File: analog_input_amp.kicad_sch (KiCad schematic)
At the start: 39 parts, among them U301 THS4521ID

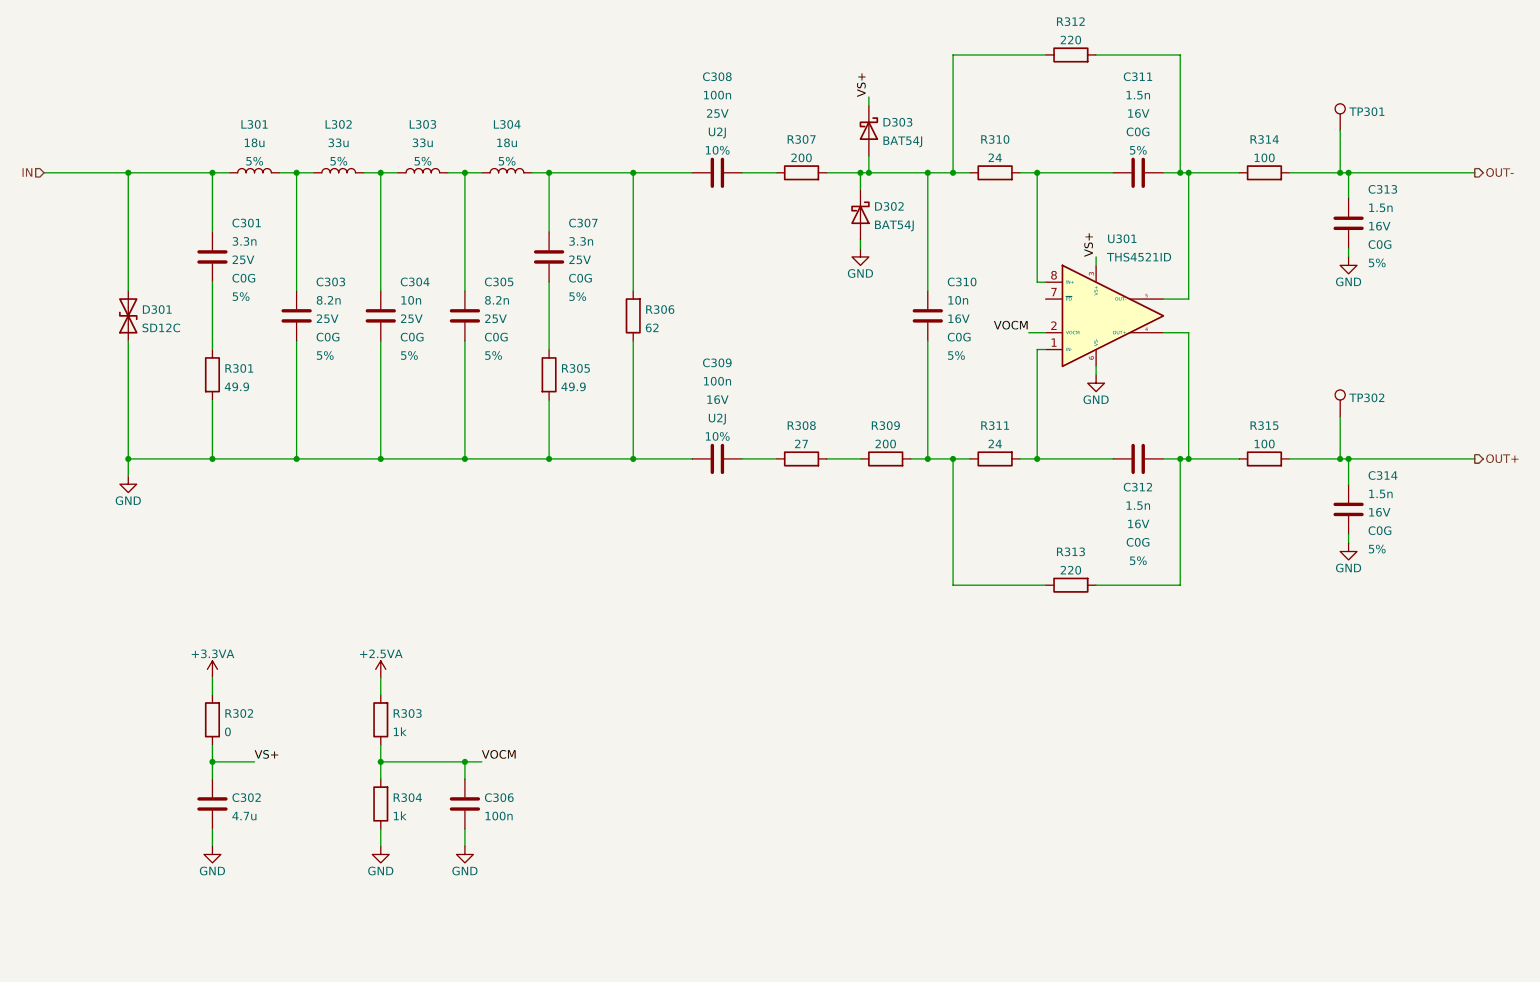
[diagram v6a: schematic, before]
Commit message: Schematic: better LDO output capacitor selection, clarified BOM
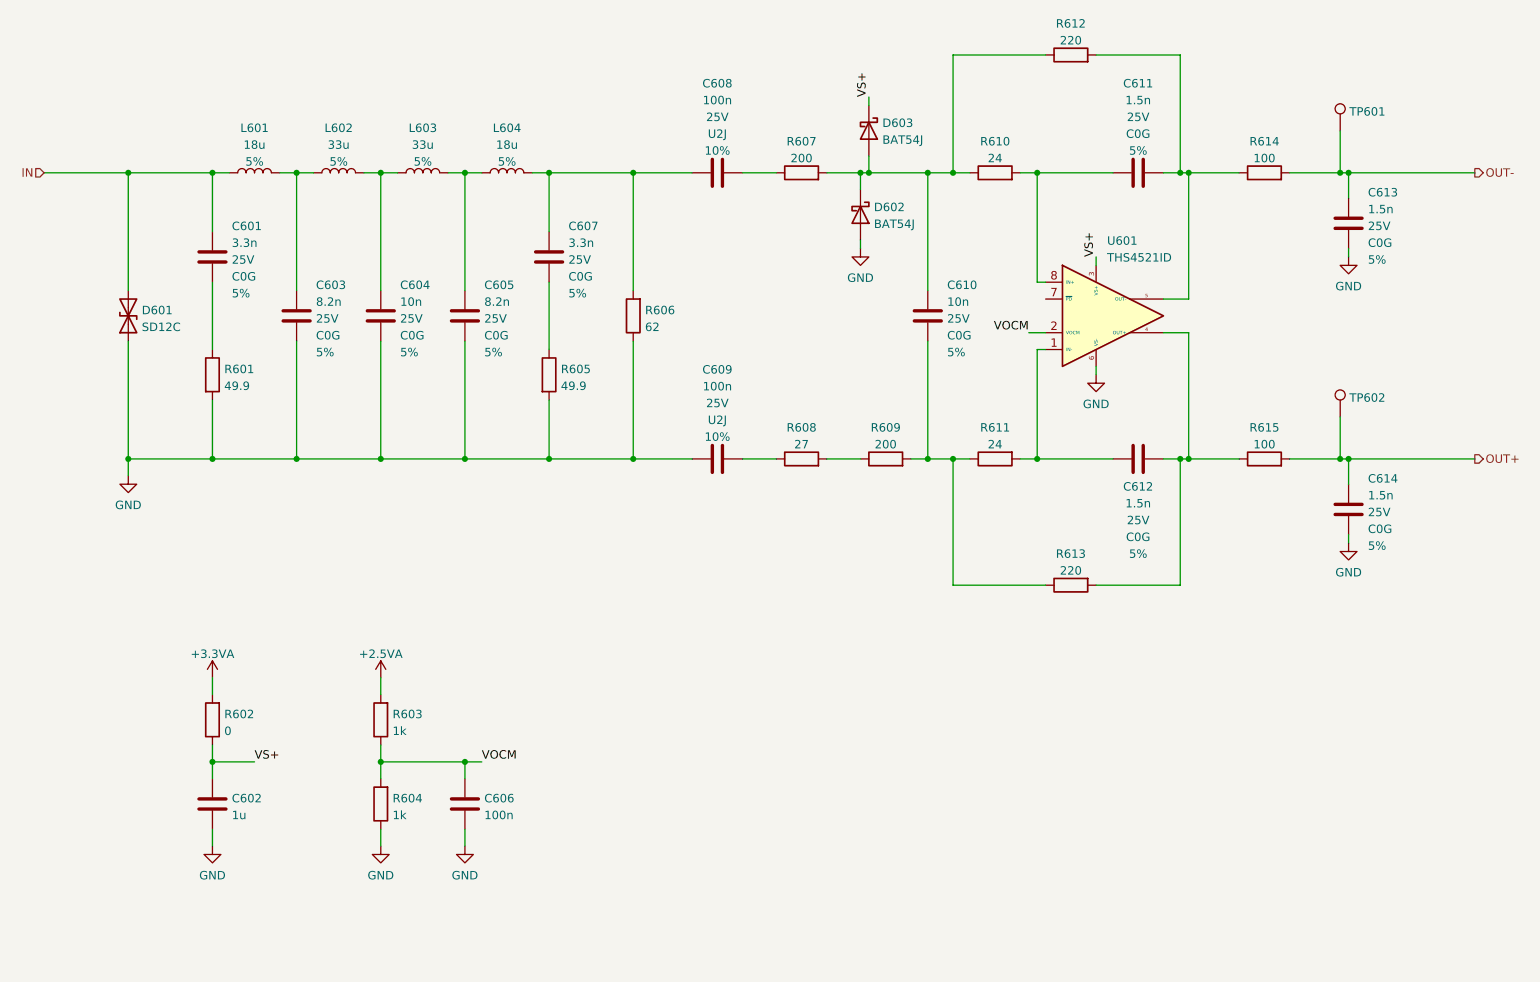
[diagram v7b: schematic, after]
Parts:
- C602: renamed from C302; value 4.7u -> 1u; Spec1 16V -> (none); Spec2 X5R -> (none); Tolerance 20% -> (none)
- C606: renamed from C306; Spec1 16V -> (none); Spec2 X5R -> (none); Tolerance 20% -> (none)
- C609: renamed from C309; Spec1 16V -> 25V
- C610: renamed from C310; Spec1 16V -> 25V
- C611: renamed from C311; Spec1 16V -> 25V
- C612: renamed from C312; Spec1 16V -> 25V
- C613: renamed from C313; Spec1 16V -> 25V
- C614: renamed from C314; Spec1 16V -> 25V
- renumbered C301 to C601, C303 to C603, C304 to C604, C305 to C605, C307 to C607, C308 to C608, D301 to D601, D302 to D602, D303 to D603, L301 to L601, L302 to L602, L303 to L603, L304 to L604, R301 to R601, R302 to R602, R303 to R603, R304 to R604, R305 to R605, R306 to R606, R307 to R607, R308 to R608, R309 to R609, R310 to R610, R311 to R611, R312 to R612, R313 to R613, R314 to R614, R315 to R615, TP301 to TP601, TP302 to TP602, U301 to U601

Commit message: Schematic: yet another update -Improve way caps are specified once again -Update cap voltages based on ESD simulation -Make anti-aliasing LC filter more practical - with much less inductors -Specify Mfr & MfrPN for almost all components (most from Mouser, some from Digikey)
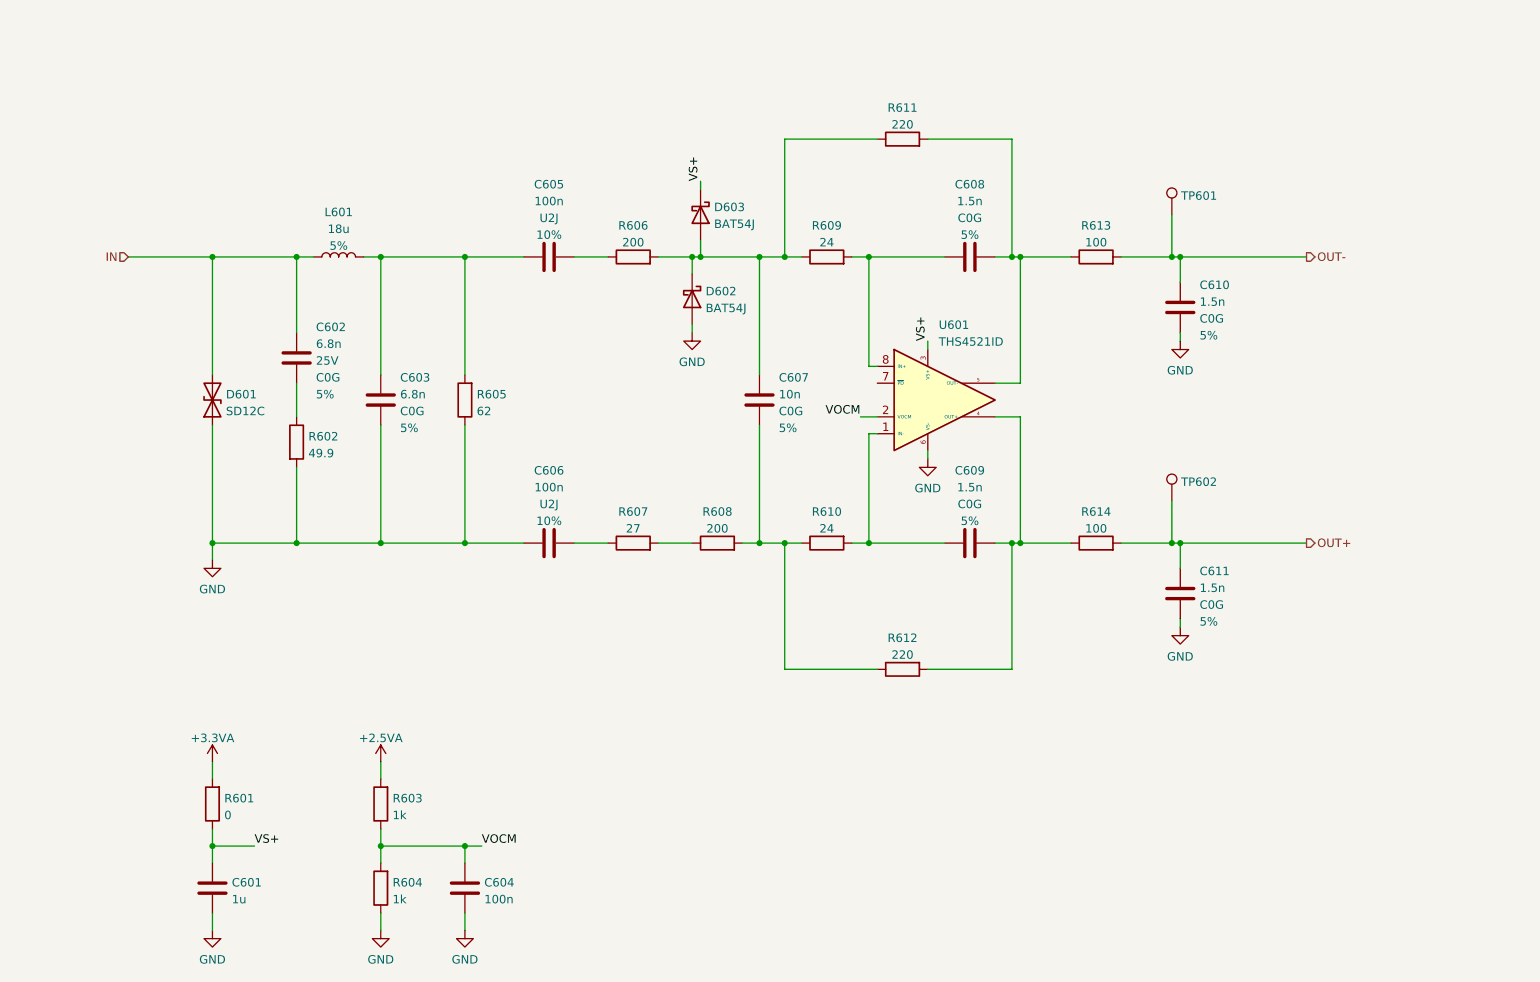
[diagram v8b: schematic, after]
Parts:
- removed C601: 3.3n, Capacitor_SMD:C_0805_2012Metric, symbol Device:C
- removed C603: 8.2n, Capacitor_SMD:C_0805_2012Metric, symbol Device:C
- removed C604: 10n, Capacitor_SMD:C_0805_2012Metric, symbol Device:C
- removed L601: 18u, symbol Device:L
- removed L602, L603: 33u, symbol Device:L
- removed R601: 49.9, Resistor_SMD:R_0805_2012Metric, symbol Device:R
- C601: renamed from C602; Mfr (none) -> Samsung; Mfr PN (none) -> CL21B105KOFNNNG
- C602: renamed from C605; value 8.2n -> 6.8n; Mfr (none) -> Murata; Mfr PN (none) -> GRM2165C2A682JA01
- C603: renamed from C607; value 3.3n -> 6.8n; Mfr (none) -> Murata; Mfr PN (none) -> GRM2165C2A682JA01; Spec1 25V -> (none)
- C604: renamed from C606; Mfr (none) -> Samsung; Mfr PN (none) -> CL21B104KBFNNNE
- C605: renamed from C608; Mfr (none) -> KEMET; Mfr PN (none) -> C1206C104K5JACTU; Spec1 25V -> (none)
- C606: renamed from C609; Mfr (none) -> KEMET; Mfr PN (none) -> C1206C104K5JACTU; Spec1 25V -> (none)
- C607: renamed from C610; Mfr (none) -> Murata; Mfr PN (none) -> GRM2165C2A103JA01; Spec1 25V -> (none)
- C608: renamed from C611; Mfr (none) -> KEMET; Mfr PN (none) -> C0805C152J5GAC; Spec1 25V -> (none)
- C609: renamed from C612; Mfr (none) -> KEMET; Mfr PN (none) -> C0805C152J5GAC; Spec1 25V -> (none)
- C610: renamed from C613; Mfr (none) -> KEMET; Mfr PN (none) -> C0805C152J5GAC; Spec1 25V -> (none)
- C611: renamed from C614; Mfr (none) -> KEMET; Mfr PN (none) -> C0805C152J5GAC; Spec1 25V -> (none)
- D601: footprint (none) -> Diode_SMD:D_SOD-323_HandSoldering; Mfr (none) -> DIODES; Mfr PN (none) -> SD12C-7
- D602, D603: footprint Diode_SMD:D_SOD-323F -> Diode_SMD:D_SOD-323_HandSoldering; Mfr (none) -> Nexperia; Mfr PN (none) -> BAT54HGWX
- L601: renamed from L604; footprint (none) -> Inductor_SMD:L_1812_4532Metric_Pad1.30x3.40mm_HandSolder; Mfr (none) -> Vishay; Mfr PN (none) -> ISC1812ES180J
- R602: renamed from R605; Tolerance 5% -> (none)
- R603, R604: Tolerance 5% -> (none)
- R605: renamed from R606; Tolerance 5% -> (none)
- R606: renamed from R607; Tolerance 5% -> (none)
- R607: renamed from R608; Tolerance 5% -> (none)
- R608: renamed from R609; Tolerance 5% -> (none)
- R609: renamed from R610; Tolerance 5% -> (none)
- R610: renamed from R611; Tolerance 5% -> (none)
- R611: renamed from R612; Tolerance 5% -> (none)
- R612: renamed from R613; Tolerance 5% -> (none)
- R613: renamed from R614; Tolerance 5% -> (none)
- R614: renamed from R615; Tolerance 5% -> (none)
- U601: Mfr (none) -> Texas Instruments; Mfr PN (none) -> THS4521IDR
- renumbered R602 to R601
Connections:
- net GND: now also C603.2; no longer C602.2
- net IN: now also C602.1, L601.1
- net at R602.1: now also C602.2; no longer C603.2
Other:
- moved on the sheet: C601, C602, C603, C604, C605, C606, C607, C608, C609, C610, C611, D601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
